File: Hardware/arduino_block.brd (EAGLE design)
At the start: 30.5 x 62.2 mm, 40 parts, among them U1 MIC5205-3.3V (150mA), U2 EDISON_CONNECTOR_FULLMOUNTING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, U3 EDISON_CONNECTOR_FULLHEADER, U4 ATMEGA328, Y1 8MHZ

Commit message: file cleanup
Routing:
- net VIN: track 83.2 -> 84.3 mm
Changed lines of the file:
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@@
 <setting verticaltext="up"/>
 </settings>
-<grid distance="0.05" unitdist="inch" unit="inch" style="lines" multiple="1" display="yes" altdistance="0.001" altunitdist="inch" altunit="inch"/>
+<grid distance="0.005" unitdist="inch" unit="inch" style="lines" multiple="1" display="yes" altdistance="0.001" altunitdist="inch" altunit="inch"/>
 <layers>
 <layer number="1" name="Top" color="4" fill="1" visible="yes" active="yes"/>
@@
 <wire x1="23.32" y1="22.5798" x2="23.32" y2="22.1798" width="0.2" layer="1"/>
 <wire x1="23.32" y1="22.9798" x2="23.32" y2="22.58" width="0.2" layer="1"/>
-<via x="22.1816" y="23.2658" extent="1-16" drill="0.3302"/>
+<via x="22.1562" y="23.2658" extent="1-16" drill="0.3302"/>
 <contactref element="U2" pad="6"/>
 <contactref element="U2" pad="2"/>
@@
 <wire x1="16.8656" y1="19.8882" x2="20.2432" y2="23.2658" width="0.254" layer="1"/>
 <wire x1="14.6812" y1="7.62" x2="16.8656" y2="9.8044" width="0.254" layer="16"/>
-<wire x1="23.32" y1="22.98" x2="22.4674" y2="22.98" width="0.1524" layer="16"/>
-<wire x1="22.4674" y1="22.98" x2="22.1816" y2="23.2658" width="0.1524" layer="16"/>
-<wire x1="22.1816" y1="23.2658" x2="22.4676" y2="22.9798" width="0.1524" layer="1"/>
-<wire x1="22.4676" y1="22.9798" x2="23.32" y2="22.9798" width="0.1524" layer="1"/>
-<wire x1="20.2432" y1="23.2658" x2="22.1816" y2="23.2658" width="0.254" layer="1"/>
+<wire x1="23.32" y1="22.98" x2="22.442" y2="22.98" width="0.1524" layer="16"/>
+<wire x1="22.442" y1="22.98" x2="22.1562" y2="23.2658" width="0.1524" layer="16"/>
+<wire x1="22.1562" y1="23.2658" x2="22.4422" y2="22.9798" width="0.1524" layer="1"/>
+<wire x1="22.4422" y1="22.9798" x2="23.32" y2="22.9798" width="0.1524" layer="1"/>
+<wire x1="20.2432" y1="23.2658" x2="22.1562" y2="23.2658" width="0.254" layer="1"/>
 <contactref element="SJ5" pad="2"/>
 <wire x1="17.78" y1="22.04" x2="18.103" y2="22.04" width="0.1524" layer="16"/>
 <wire x1="18.103" y1="22.04" x2="19.3288" y2="23.2658" width="0.1524" layer="16"/>
-<wire x1="19.3288" y1="23.2658" x2="22.1816" y2="23.2658" width="0.1524" layer="16"/>
+<wire x1="19.3288" y1="23.2658" x2="22.1562" y2="23.2658" width="0.1524" layer="16"/>
 </signal>
 <signal name="3.3V">
@@
 <wire x1="23.3194" y1="20.9804" x2="24.1554" y2="20.9804" width="0.2032" layer="1"/>
 <wire x1="24.1554" y1="20.9804" x2="24.257" y2="21.082" width="0.2032" layer="1"/>
-<wire x1="24.257" y1="21.082" x2="24.257" y2="23.241" width="0.2032" layer="1"/>
+<wire x1="24.257" y1="21.082" x2="24.257" y2="23.495" width="0.2032" layer="1"/>
 <wire x1="8.89" y1="20.32" x2="9.779" y2="20.32" width="0.2032" layer="1"/>
 <wire x1="14.23" y1="12.7" x2="10.668" y2="12.7" width="0.2032" layer="1"/>
@@
 <wire x1="22.1742" y1="21.3106" x2="22.505" y2="20.9798" width="0.1524" layer="1"/>
 <wire x1="22.505" y1="20.9798" x2="23.32" y2="20.9798" width="0.1524" layer="1"/>
-<wire x1="18.8722" y1="23.9522" x2="23.5458" y2="23.9522" width="0.2032" layer="1"/>
-<wire x1="23.5458" y1="23.9522" x2="24.257" y2="23.241" width="0.2032" layer="1"/>
+<wire x1="18.8722" y1="23.9522" x2="23.7998" y2="23.9522" width="0.2032" layer="1"/>
+<wire x1="23.7998" y1="23.9522" x2="24.257" y2="23.495" width="0.2032" layer="1"/>
 </signal>
 <signal name="FW_RCVR">
@@
 <wire x1="14.0001" y1="5.4" x2="14.417" y2="5.4" width="0.254" layer="1"/>
 <wire x1="16.51" y1="4.95" x2="16.51" y2="6.35" width="0.254" layer="1"/>
-<wire x1="0.508" y1="43.307" x2="0.508" y2="8.382" width="0.3556" layer="16"/>
 <wire x1="0.508" y1="8.382" x2="5.08" y2="3.81" width="0.3556" layer="16"/>
 <wire x1="5.08" y1="3.81" x2="15.37" y2="3.81" width="0.3556" layer="16"/>
@@
 <wire x1="1.27" y1="44.069" x2="1.524" y2="44.069" width="0.3556" layer="16"/>
 <wire x1="1.524" y1="44.069" x2="2.54" y2="45.085" width="0.3556" layer="16"/>
+<wire x1="0.508" y1="43.307" x2="0.508" y2="39.624" width="0.3556" layer="16"/>
+<wire x1="0.508" y1="39.624" x2="1.778" y2="38.354" width="0.3556" layer="16"/>
+<wire x1="1.778" y1="38.354" x2="1.778" y2="37.338" width="0.3556" layer="16"/>
+<wire x1="1.778" y1="37.338" x2="0.508" y2="36.068" width="0.3556" layer="16"/>
+<wire x1="0.508" y1="36.068" x2="0.508" y2="8.382" width="0.3556" layer="16"/>
 </signal>
 <signal name="ARD_DTR">

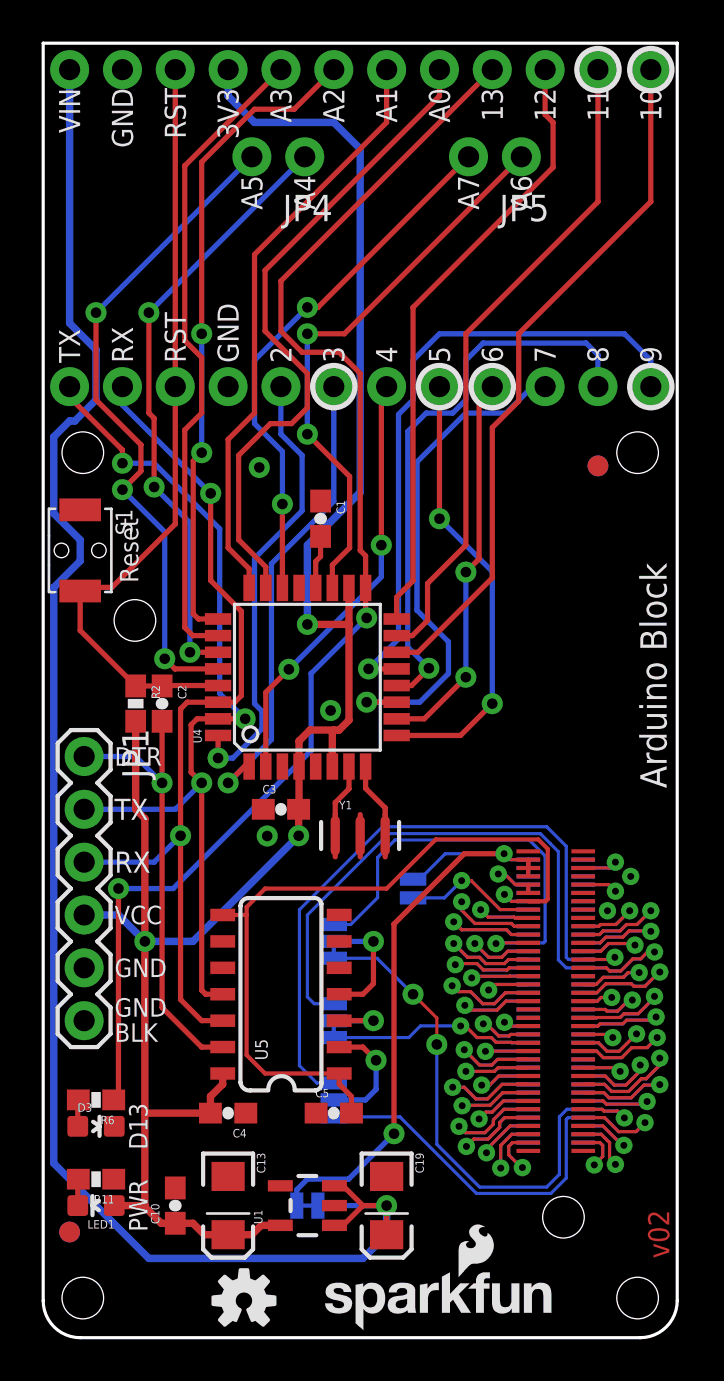
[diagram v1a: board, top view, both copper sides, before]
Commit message: updating connector packages. Fixing silk.
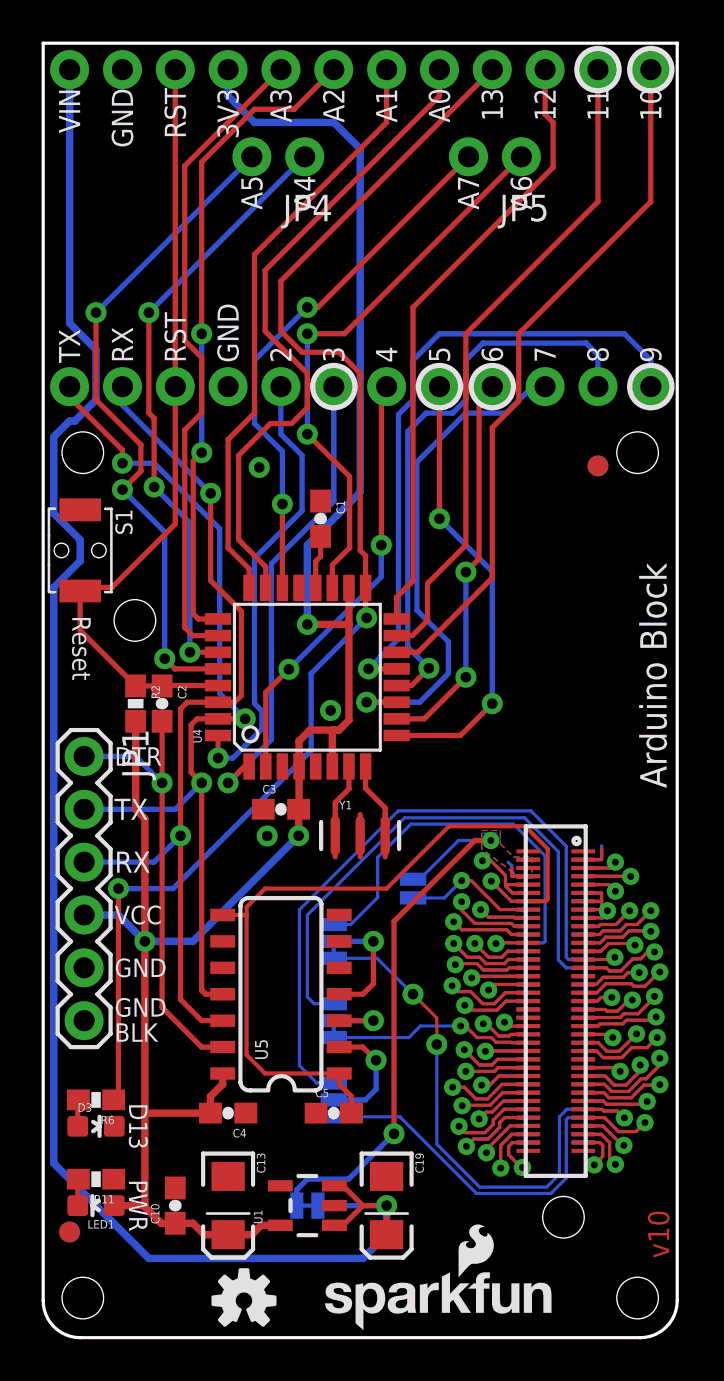
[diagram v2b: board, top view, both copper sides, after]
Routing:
- net GND: track 0.00 -> 16.5 mm
- net 3.3V: track 4.11 -> 8.51 mm
- net 1.8V: track 37.2 -> 39.5 mm
- net VSYS: track 32.8 -> 31.2 mm
- net GP135_UART_2_TX: track 33.7 -> 34.3 mm
- net GP134_UART_2_RX: track 21.4 -> 22.0 mm
- net GP165: track 33.7 -> 34.3 mm
- added copper zone on layer 1, net VSYS
- added copper zone on layer 16, net VSYS
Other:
- board text added: "v10"
- board text removed: "v02"

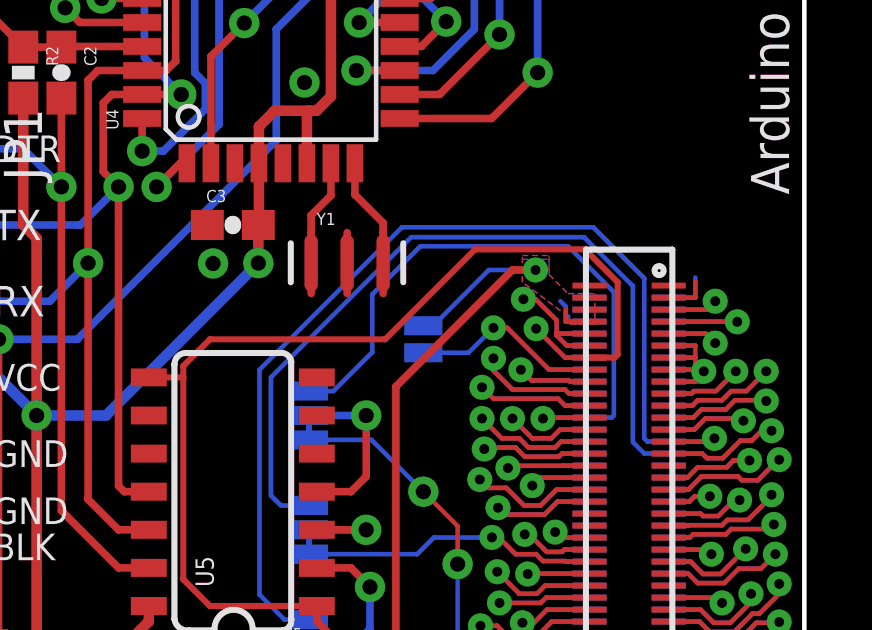
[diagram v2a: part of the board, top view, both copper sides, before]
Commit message: fixing silk directions on bottom
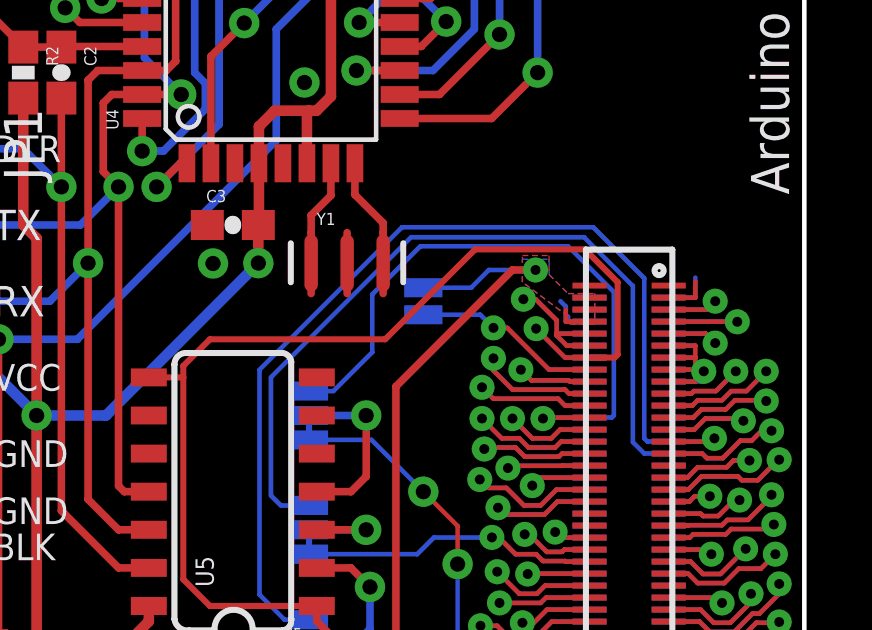
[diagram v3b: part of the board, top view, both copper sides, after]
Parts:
- moved SJ5 1.27 mm to (17.8, 22.9)
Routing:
- net VSYS: track 31.2 -> 30.6 mm
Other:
- board text removed: "Cut this jumper if you supply VIN externally!"

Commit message: adjusting a few traces, relocating a jumper
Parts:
- moved SJ5 3.81 mm to (14.0, 22.9)
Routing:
- net DCIN: track 10.1 -> 13.9 mm
- net VSYS: track 30.6 -> 34.4 mm
- net GP134_UART_2_RX: track 22.0 -> 25.5 mm
- net GP165: track 34.3 -> 37.1 mm
- net GP135_UART_2_TX: track 34.3 -> 37.1 mm
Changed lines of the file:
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@@
 <setting verticaltext="up"/>
 </settings>
-<grid distance="0.05" unitdist="inch" unit="inch" style="lines" multiple="1" display="yes" altdistance="0.005" altunitdist="inch" altunit="inch"/>
+<grid distance="0.025" unitdist="inch" unit="inch" style="lines" multiple="1" display="yes" altdistance="0.005" altunitdist="inch" altunit="inch"/>
 <layers>
 <layer number="1" name="Top" color="4" fill="1" visible="yes" active="yes"/>
@@
 <layer number="19" name="Unrouted" color="6" fill="1" visible="yes" active="yes"/>
 <layer number="20" name="Dimension" color="15" fill="1" visible="yes" active="yes"/>
-<layer number="21" name="tPlace" color="16" fill="1" visible="yes" active="yes"/>
+<layer number="21" name="tPlace" color="16" fill="1" visible="no" active="yes"/>
 <layer number="22" name="bPlace" color="14" fill="1" visible="yes" active="yes"/>
 <layer number="23" name="tOrigins" color="15" fill="1" visible="yes" active="yes"/>
@@
 <layer number="45" name="Holes" color="7" fill="1" visible="yes" active="yes"/>
 <layer number="46" name="Milling" color="3" fill="1" visible="no" active="yes"/>
-<layer number="51" name="tDocu" color="6" fill="1" visible="yes" active="yes"/>
+<layer number="51" name="tDocu" color="6" fill="1" visible="no" active="yes"/>
 <layer number="3" name="Route3" color="4" fill="3" visible="no" active="no"/>
 <layer number="4" name="Route4" color="1" fill="4" visible="no" active="no"/>
@@
 <text x="22.987" y="55.88" size="1.016" layer="21" font="vector" ratio="15" rot="R90" align="center-right">A6</text>
 <text x="29.972" y="40.132" size="1.27" layer="22" font="vector" ratio="15" rot="SMR270">Arduino Block</text>
-<text x="16.5862" y="23.4442" size="0.8128" layer="22" font="vector" ratio="15" rot="MR0" align="center-left">VSYS</text>
-<text x="16.5862" y="22.2758" size="0.8128" layer="22" font="vector" ratio="15" rot="MR0" align="center-left">DCIN</text>
+<text x="12.7762" y="23.4442" size="0.8128" layer="22" font="vector" ratio="15" rot="MR0" align="center-left">VSYS</text>
+<text x="12.7762" y="22.2758" size="0.8128" layer="22" font="vector" ratio="15" rot="MR0" align="center-left">DCIN</text>
 <dimension x1="0" y1="1.778" x2="30.48" y2="1.778" x3="15.24" y3="-5.333996875" textsize="1.778" layer="51" dtype="horizontal" unit="inch"/>
 <dimension x1="1.905" y1="1.905" x2="28.575" y2="1.905" x3="15.24" y3="-2.794" textsize="1.778" layer="51" dtype="horizontal" unit="inch"/>
@@
 <element name="JP4" library="SparkFun-Connectors" package="1X02_NO_SILK" value="M021X02_NO_SILK" x="12.573" y="56.769" rot="R180"/>
 <element name="JP5" library="SparkFun-Connectors" package="1X02_NO_SILK" value="M021X02_NO_SILK" x="22.987" y="56.769" rot="R180"/>
-<element name="SJ5" library="SparkFun-Passives" package="PAD-JUMPER-2-NO_YES_SILK" value="DCIN" x="17.78" y="22.86" rot="MR90"/>
+<element name="SJ5" library="SparkFun-Passives" package="PAD-JUMPER-2-NO_YES_SILK" value="DCIN" x="13.97" y="22.86" rot="MR90"/>
 <element name="S1" library="SparkFun-Electromechanical" package="TACTILE_SWITCH-SMD-RIGHT-ANGLE" value="RESET" x="1.778" y="37.846" rot="R270">
 <attribute name="PROD_ID" value="COMP-12265" x="1.778" y="37.846" size="1.778" layer="27" rot="R270" display="off"/>
@@
 <contactref element="C4" pad="1"/>
 <contactref element="U5" pad="7"/>
-<via x="10.7696" y="24.1173" extent="1-16" drill="0.508"/>
+<via x="10.1346" y="24.1173" extent="1-16" drill="0.508"/>
 <via x="13.8176" y="30.1498" extent="1-16" drill="0.508"/>
 <contactref element="JP2" pad="2"/>
@@
 <wire x1="20.7512" y1="23.9008" x2="21.5212" y2="23.9008" width="0.254" layer="1"/>
 <contactref element="SJ5" pad="2"/>
-<wire x1="17.78" y1="23.31" x2="19.373" y2="23.31" width="0.1524" layer="16"/>
+<wire x1="13.97" y1="23.31" x2="19.373" y2="23.31" width="0.1524" layer="16"/>
 <wire x1="19.373" y1="23.31" x2="19.9638" y2="23.9008" width="0.1524" layer="16"/>
 <wire x1="19.9638" y1="23.9008" x2="21.5212" y2="23.9008" width="0.1524" layer="16"/>
@@
 <wire x1="25.146" y1="18.288" x2="25.146" y2="23.622" width="0.1524" layer="16"/>
 <wire x1="25.146" y1="23.622" x2="23.4442" y2="25.3238" width="0.1524" layer="16"/>
-<wire x1="13.1572" y1="12.2428" x2="12.319" y2="13.081" width="0.1524" layer="16"/>
-<wire x1="12.319" y1="13.081" x2="12.319" y2="20.574" width="0.1524" layer="16"/>
-<wire x1="12.319" y1="20.574" x2="17.0688" y2="25.3238" width="0.1524" layer="16"/>
+<wire x1="13.1572" y1="12.2428" x2="11.684" y2="13.716" width="0.1524" layer="16"/>
+<wire x1="11.684" y1="13.716" x2="11.684" y2="23.749" width="0.1524" layer="16"/>
+<wire x1="11.684" y1="23.749" x2="13.2588" y2="25.3238" width="0.1524" layer="16"/>
 <contactref element="SJ3" pad="1"/>
 <wire x1="13.97" y1="12.2428" x2="13.1572" y2="12.2428" width="0.1524" layer="16"/>
-<wire x1="17.0688" y1="25.3238" x2="23.4442" y2="25.3238" width="0.1524" layer="16"/>
+<wire x1="13.2588" y1="25.3238" x2="23.4442" y2="25.3238" width="0.1524" layer="16"/>
 </signal>
 <signal name="GP44">
@@
 <wire x1="25.146" y1="17.78" x2="24.765" y2="18.161" width="0.1524" layer="16"/>
 <wire x1="24.765" y1="18.161" x2="24.765" y2="23.368" width="0.1524" layer="16"/>
-<wire x1="17.3736" y1="24.9936" x2="12.7" y2="20.32" width="0.1524" layer="16"/>
-<wire x1="12.7" y1="20.32" x2="12.7" y2="16.383" width="0.1524" layer="16"/>
-<wire x1="12.7" y1="16.383" x2="13.0302" y2="16.0528" width="0.1524" layer="16"/>
+<wire x1="13.5636" y1="24.9936" x2="12.065" y2="23.495" width="0.1524" layer="16"/>
+<wire x1="12.065" y1="23.495" x2="12.065" y2="17.018" width="0.1524" layer="16"/>
+<wire x1="12.065" y1="17.018" x2="13.0302" y2="16.0528" width="0.1524" layer="16"/>
 <contactref element="SJ1" pad="1"/>
 <wire x1="13.0302" y1="16.0528" x2="13.97" y2="16.0528" width="0.1524" layer="16"/>
-<wire x1="17.3736" y1="24.9936" x2="23.1394" y2="24.9936" width="0.1524" layer="16"/>
+<wire x1="13.5636" y1="24.9936" x2="23.1394" y2="24.9936" width="0.1524" layer="16"/>
 <wire x1="23.1394" y1="24.9936" x2="24.765" y2="23.368" width="0.1524" layer="16"/>
 </signal>
@@
 <wire x1="21.7994" y1="18.98" x2="21.7678" y2="18.9484" width="0.1524" layer="16"/>
 <contactref element="SJ2" pad="1"/>
-<wire x1="14.7828" y1="19.8628" x2="13.97" y2="19.8628" width="0.1524" layer="16"/>
-<wire x1="17.6784" y1="24.6888" x2="22.606" y2="24.6888" width="0.1524" layer="16"/>
+<wire x1="13.7668" y1="24.6888" x2="22.606" y2="24.6888" width="0.1524" layer="16"/>
 <wire x1="22.606" y1="24.6888" x2="24.13" y2="23.1648" width="0.1524" layer="16"/>
-<wire x1="17.6784" y1="24.6888" x2="16.0782" y2="23.0886" width="0.1524" layer="16"/>
-<wire x1="16.0782" y1="23.0886" x2="16.0782" y2="21.1582" width="0.1524" layer="16"/>
-<wire x1="16.0782" y1="21.1582" x2="14.7828" y2="19.8628" width="0.1524" layer="16"/>
+<wire x1="13.7668" y1="24.6888" x2="12.446" y2="23.368" width="0.1524" layer="16"/>
+<wire x1="12.446" y1="23.368" x2="12.446" y2="20.701" width="0.1524" layer="16"/>
+<wire x1="12.446" y1="20.701" x2="13.2842" y2="19.8628" width="0.1524" layer="16"/>
+<wire x1="13.97" y1="19.8628" x2="13.2842" y2="19.8628" width="0.1524" layer="16"/>
 </signal>
 <signal name="GP43_I2S_2_TXD">
@@
 <via x="4.8895" y="19.05" extent="1-16" drill="0.508"/>
 <wire x1="4.445" y1="29.63" x2="4.445" y2="25.4" width="0.3556" layer="1"/>
-<wire x1="12.28" y1="25.4" x2="12.28" y2="24.13" width="0.3556" layer="1"/>
-<via x="12.28" y="24.13" extent="1-16" drill="0.508"/>
+<via x="9.486" y="21.717" extent="1-16" drill="0.508"/>
 <wire x1="3.417" y1="6.35" x2="4.8895" y2="6.35" width="0.3556" layer="1"/>
 <wire x1="8.63" y1="12.7" x2="8.63" y2="12.186" width="0.3556" layer="1"/>
@@
 <wire x1="8.04" y1="10.795" x2="4.8895" y2="10.795" width="0.3556" layer="1"/>
 <wire x1="4.8895" y1="19.05" x2="4.8895" y2="24.9555" width="0.3556" layer="1"/>
-<wire x1="4.8895" y1="19.05" x2="7.2" y2="19.05" width="0.3556" layer="16"/>
-<wire x1="7.2" y1="19.05" x2="12.28" y2="24.13" width="0.3556" layer="16"/>
 <wire x1="12.7" y1="34.29" x2="12.7" y2="38.1" width="0.3556" layer="16"/>
 <wire x1="12.7" y1="38.1" x2="15.24" y2="40.64" width="0.3556" layer="16"/>
@@
 <wire x1="13.97" y1="58.42" x2="10.16" y2="58.42" width="0.3556" layer="16"/>
 <wire x1="10.16" y1="58.42" x2="8.89" y2="59.69" width="0.3556" layer="16"/>
+<wire x1="12.28" y1="25.4" x2="12.28" y2="24.511" width="0.3556" layer="1"/>
+<wire x1="12.28" y1="24.511" x2="9.486" y2="21.717" width="0.3556" layer="1"/>
+<wire x1="9.486" y1="21.717" x2="6.819" y2="19.05" width="0.3556" layer="16"/>
+<wire x1="6.819" y1="19.05" x2="4.8895" y2="19.05" width="0.3556" layer="16"/>
 </signal>
 <signal name="D9">
@@
 <wire x1="20.579" y1="21.971" x2="20.1168" y2="21.971" width="0.1524" layer="16"/>
 <contactref element="SJ5" pad="1"/>
-<wire x1="17.78" y1="22.41" x2="19.6778" y2="22.41" width="0.1524" layer="16"/>
+<wire x1="13.97" y1="22.41" x2="19.6778" y2="22.41" width="0.1524" layer="16"/>
 <wire x1="19.6778" y1="22.41" x2="20.1168" y2="21.971" width="0.1524" layer="16"/>
 </signal>
